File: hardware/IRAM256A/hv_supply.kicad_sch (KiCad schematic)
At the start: 32 parts

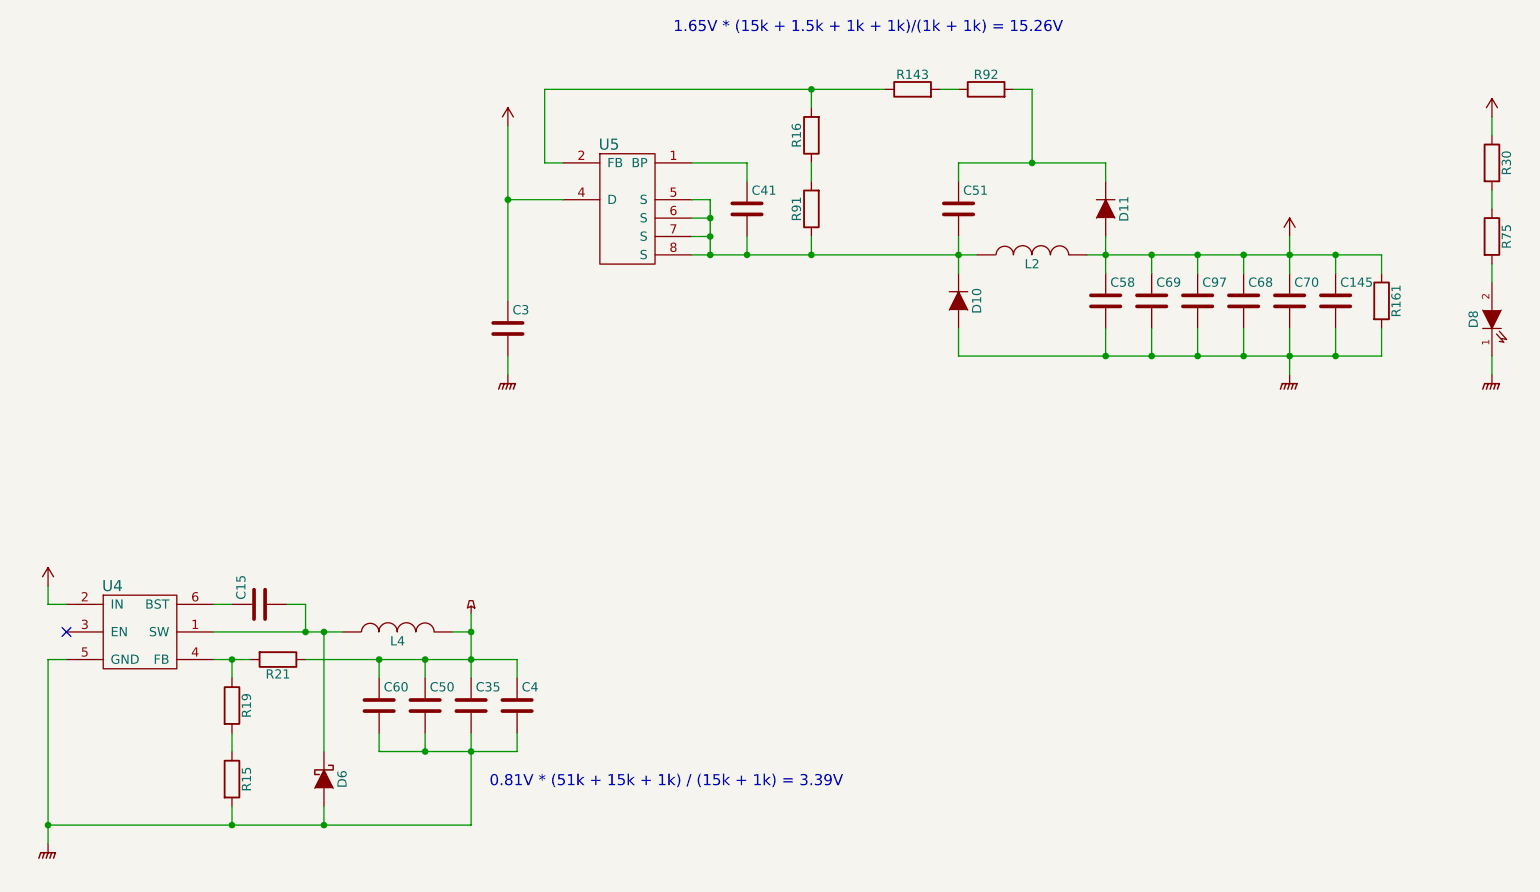
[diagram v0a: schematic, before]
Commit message: Structure change + kicad 3d models updated
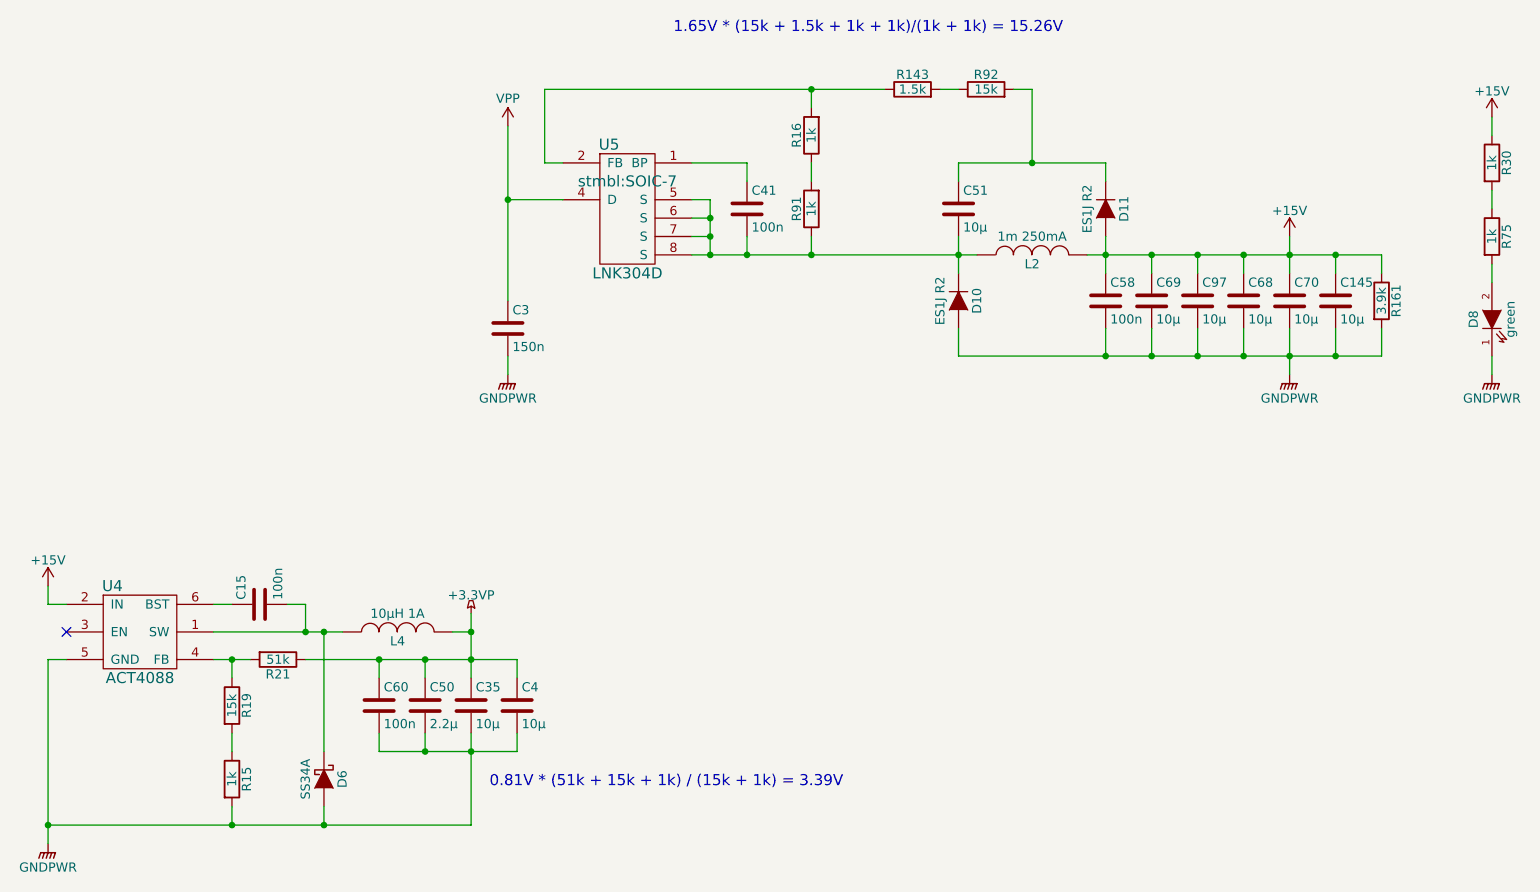
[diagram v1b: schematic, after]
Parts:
- C145, C35, C4, C51, C68, C69, C70, C97: value (none) -> 10µ; footprint (none) -> stmbl:C_0805
- C15, C41, C58, C60: value (none) -> 100n; footprint (none) -> stmbl:C_0603
- C3: value (none) -> 150n; footprint (none) -> stmbl:C_1808
- C50: value (none) -> 2.2µ; footprint (none) -> stmbl:C_0603
- D10, D11: value (none) -> ES1J R2; footprint (none) -> stmbl:SMA_Standard
- D6: value (none) -> SS34A; footprint (none) -> stmbl:SMA_Standard
- D8: value (none) -> green; footprint (none) -> stmbl:LED-0805-SIDE
- L2: value (none) -> 1m 250mA; footprint (none) -> stmbl:NPI31W
- L4: value (none) -> 10µH 1A; footprint (none) -> stmbl:SMD_INDUCTOR_32x25
- R143: value (none) -> 1.5k; footprint (none) -> stmbl:R_0603
- R15, R16, R30, R75, R91: value (none) -> 1k; footprint (none) -> stmbl:R_0603
- R161: value (none) -> 3.9k; footprint (none) -> stmbl:R_0603
- R19, R92: value (none) -> 15k; footprint (none) -> stmbl:R_0603
- R21: value (none) -> 51k; footprint (none) -> stmbl:R_0603
- U4: value (none) -> ACT4088; footprint (none) -> stmbl:SOT-23-6
- U5: value (none) -> LNK304D; footprint (none) -> stmbl:SOIC-7

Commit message: intermediate update
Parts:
- U4: value ACT4088 -> AOZ1280; footprint stmbl:SOT-23-6 -> Package_TO_SOT_SMD:SOT-23-6; symbol stmbl_4.0-rescue:ACT4088-stmbl -> stmbl:AOZ1280
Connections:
- net +15V: now also U4.5 (IN); no longer U4.2 (IN)
- net GNDPWR: now also U4.2 (GND); no longer U4.5 (GND)
- net at R19.1, R21.2: now also U4.3 (FB); no longer U4.4 (FB)
- net at C15.2, D6.1 (K), L4.1: now also U4.6 (LX); no longer U4.1 (SW)
- net at C15.1: now also U4.1 (BST); no longer U4.6 (BST)
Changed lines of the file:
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@@
     (pin "2")
   )
-  (symbol (lib_id "stmbl_4.0-rescue:ACT4088-stmbl") (at 49.53 153.67 0) (unit 1)
+  (symbol (lib_id "stmbl:AOZ1280") (at 49.53 153.67 0) (unit 1)
     (in_bom yes) (on_board yes)
     (property "Reference" "U4" (id 0) (at 45.72 147.32 0)
       (effects (font (size 1.524 1.524)))
     )
-    (property "Value" "ACT4088" (id 1) (at 49.53 160.02 0)
+    (property "Value" "AOZ1280" (id 1) (at 49.53 160.02 0)
       (effects (font (size 1.524 1.524)))
     )
-    (property "Footprint" "stmbl:SOT-23-6" (id 2) (at 49.53 153.67 0)
+    (property "Footprint" "Package_TO_SOT_SMD:SOT-23-6" (id 2) (at 49.53 153.67 0)
       (effects (font (size 1.524 1.524)) hide)
     )
-    (property "Datasheet" "" (id 3) (at 49.53 153.67 0)
-      (effects (font (size 1.524 1.524)))
+    (property "Datasheet" "https://www.tme.eu/Document/921be39cd2271a5b3bfe03eff0ec2438/AOZ1280CI-DTE.pdf" (id 3) (at 49.53 153.67 0)
+      (effects (font (size 1.524 1.524)) hide)
     )
     (property "InternalName" "" (id 4) (at 49.53 153.67 0)
